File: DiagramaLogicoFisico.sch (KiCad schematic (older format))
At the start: 46 parts, among them J1 Conn_01x02_Servo1, J10 Conn_01x04_TRIS, J11 Conn_01x02_DSP, J2 Conn_01x03_UART1, J3 Conn_01x03_UART2, J4 Conn_01x04_PWM, J5 Conn_01x05_PROGRAMER, J6 Conn_01x02_POWER, J7 Conn_01x02_Servo2, J8 Conn_01x02_Servo3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

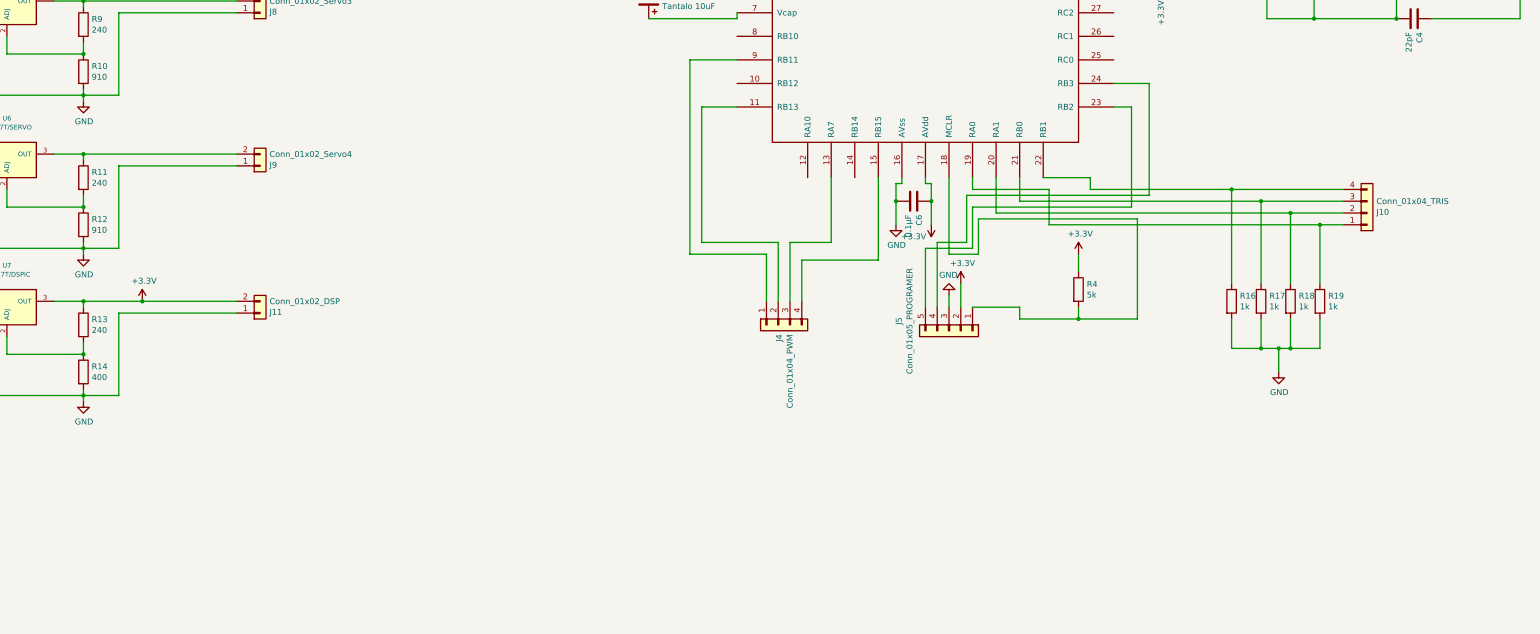
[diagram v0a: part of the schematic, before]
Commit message: Añadido los circuitos de interruptores y sus pines de alimentación
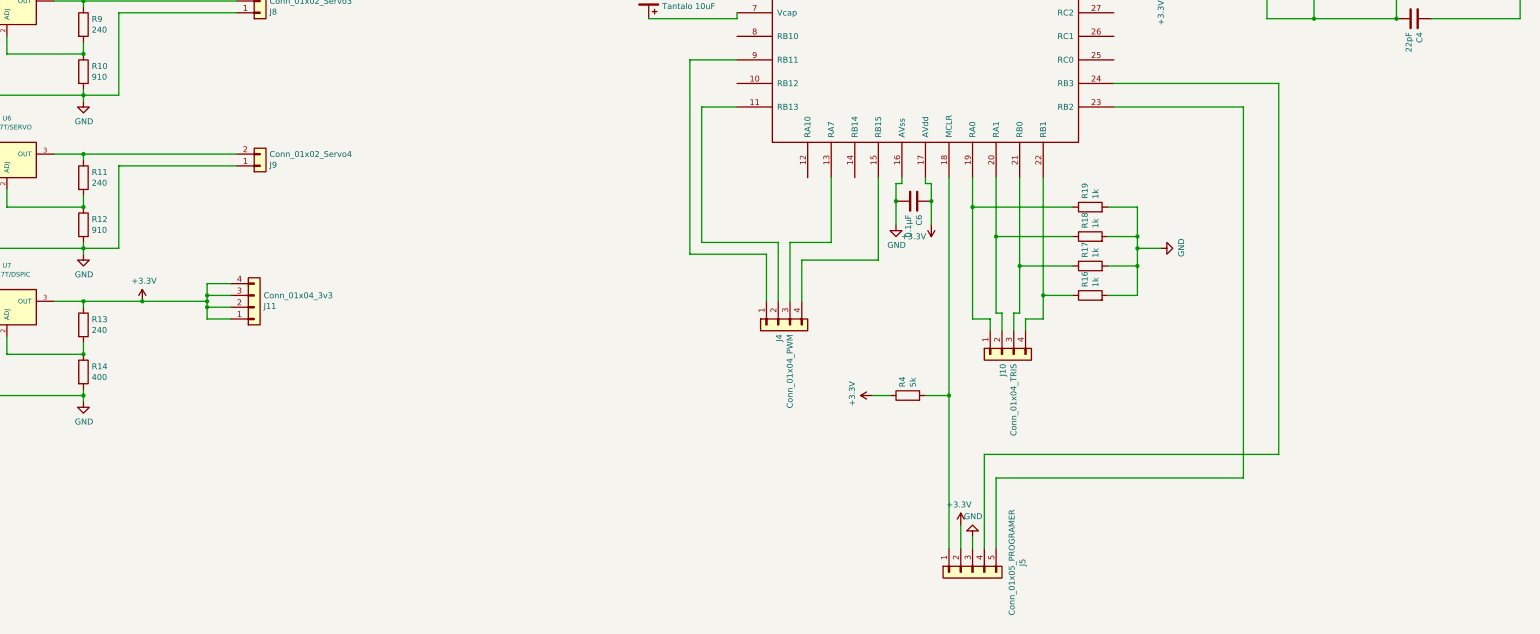
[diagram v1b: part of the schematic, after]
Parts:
- removed J11: Conn_01x02_DSP, TerminalBlock:TerminalBlock_bornier-2_P5.08mm, symbol Connector_Generic:Conn_01x02
- added J11: Conn_01x04_3v3, Connector_PinHeader_2.54mm:PinHeader_1x04_P2.54mm_Vertical, symbol Connector_Generic:Conn_01x04
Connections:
- net +3V3: now also J11.1 (Pin_1), J11.2 (Pin_2), J11.3 (Pin_3), J11.4 (Pin_4)
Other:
- moved on the sheet: J10, J5, R16, R17, R18, R19, R4

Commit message: añadidas algunas modifiaciones
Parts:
- added J?: Conn_01x04_TRIS, Connector_PinHeader_2.54mm:PinHeader_1x04_P2.54mm_Vertical, symbol Connector_Generic:Conn_01x04
- added JP? (x4): Jumper, symbol Device:Jumper
- added R? (x4): 1k, Resistor_THT:R_Axial_DIN0204_L3.6mm_D1.6mm_P5.08mm_Horizontal, symbol Device:R
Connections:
- net +3V3: now also JP?.1, JP?.1, JP?.1, JP?.1
- net GND: now also J?.1 (Pin_1), J?.2 (Pin_2), J?.3 (Pin_3), J?.4 (Pin_4), R?.1, R?.1, R?.1, R?.1
- new net: JP?.2, R?.2 (x4)
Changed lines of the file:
@@
 	10400 14150 10400 14250
 Connection ~ 10400 14250
+$Comp
+L Device:Jumper JP?
+U 1 1 5EFD7640
+P 21950 3550
+F 0 "JP?" H 21950 3814 50  0000 C CNN
+F 1 "Jumper" H 21950 3723 50  0000 C CNN
+F 2 "" H 21950 3550 50  0001 C CNN
+F 3 "~" H 21950 3550 50  0001 C CNN
+	1    21950 3550
+	0    1    1    0
+$EndComp
+$Comp
+L power:GND #PWR?
+U 1 1 5EFF4984
+P 22750 4900
+F 0 "#PWR?" H 22750 4650 50  0001 C CNN
+F 1 "GND" H 22755 4727 50  0000 C CNN
+F 2 "" H 22750 4900 50  0001 C CNN
+F 3 "" H 22750 4900 50  0001 C CNN
+	1    22750 4900
+	1    0    0    -1
+$EndComp
+$Comp
+L Device:R R?
+U 1 1 5F003B7F
+P 21950 4150
+F 0 "R?" H 22020 4196 50  0000 L CNN
+F 1 "1k" H 22020 4105 50  0000 L CNN
+F 2 "Resistor_THT:R_Axial_DIN0204_L3.6mm_D1.6mm_P5.08mm_Horizontal" V 21880 4150 50  0001 C CNN
+F 3 "~" H 21950 4150 50  0001 C CNN
+	1    21950 4150
+	-1   0    0    1
+$EndComp
+Wire Wire Line
+	21950 4000 21950 3850
+$Comp
+L power:+3.3V #PWR?
+U 1 1 5F085C7E
+P 22750 2900
+F 0 "#PWR?" H 22750 2750 50  0001 C CNN
+F 1 "+3.3V" H 22900 3000 50  0000 C CNN
+F 2 "" H 22750 2900 50  0001 C CNN
+F 3 "" H 22750 2900 50  0001 C CNN
+	1    22750 2900
+	1    0    0    -1
+$EndComp
+$Comp
+L Device:Jumper JP?
+U 1 1 5F0B49E5
+P 22500 3550
+F 0 "JP?" H 22500 3814 50  0000 C CNN
+F 1 "Jumper" H 22500 3723 50  0000 C CNN
+F 2 "" H 22500 3550 50  0001 C CNN
+F 3 "~" H 22500 3550 50  0001 C CNN
+	1    22500 3550
+	0    1    1    0
+$EndComp
+$Comp
+L Device:R R?
+U 1 1 5F0B49EB
+P 22500 4150
+F 0 "R?" H 22570 4196 50  0000 L CNN
+F 1 "1k" H 22570 4105 50  0000 L CNN
+F 2 "Resistor_THT:R_Axial_DIN0204_L3.6mm_D1.6mm_P5.08mm_Horizontal" V 22430 4150 50  0001 C CNN
+F 3 "~" H 22500 4150 50  0001 C CNN
+	1    22500 4150
+	-1   0    0    1
+$EndComp
+Wire Wire Line
+	22500 4000 22500 3850
+$Comp
+L Device:Jumper JP?
+U 1 1 5F0C321D
+P 22950 3550
+F 0 "JP?" H 22950 3814 50  0000 C CNN
+F 1 "Jumper" H 22950 3723 50  0000 C CNN
+F 2 "" H 22950 3550 50  0001 C CNN
+F 3 "~" H 22950 3550 50  0001 C CNN
+	1    22950 3550
+	0    1    1    0
+$EndComp
+$Comp
+L Device:R R?
+U 1 1 5F0C3223
+P 22950 4150
+F 0 "R?" H 23020 4196 50  0000 L CNN
+F 1 "1k" H 23020 4105 50  0000 L CNN
+F 2 "Resistor_THT:R_Axial_DIN0204_L3.6mm_D1.6mm_P5.08mm_Horizontal" V 22880 4150 50  0001 C CNN
+F 3 "~" H 22950 4150 50  0001 C CNN
+	1    22950 4150
+	-1   0    0    1
+$EndComp
+Wire Wire Line
+	22950 4000 22950 3850
+$Comp
+L Device:Jumper JP?
+U 1 1 5F0D216C
+P 23350 3550
+F 0 "JP?" H 23350 3814 50  0000 C CNN
+F 1 "Jumper" H 23350 3723 50  0000 C CNN
+F 2 "" H 23350 3550 50  0001 C CNN
+F 3 "~" H 23350 3550 50  0001 C CNN
+	1    23350 3550
+	0    1    1    0
+$EndComp
+$Comp
+L Device:R R?
+U 1 1 5F0D2172
+P 23350 4150
+F 0 "R?" H 23420 4196 50  0000 L CNN
+F 1 "1k" H 23420 4105 50  0000 L CNN
+F 2 "Resistor_THT:R_Axial_DIN0204_L3.6mm_D1.6mm_P5.08mm_Horizontal" V 23280 4150 50  0001 C CNN
+F 3 "~" H 23350 4150 50  0001 C CNN
+	1    23350 4150
+	-1   0    0    1
+$EndComp
+Wire Wire Line
+	23350 4000 23350 3850
+Wire Wire Line
+	22750 2900 22500 2900
+Wire Wire Line
+	21950 2900 21950 3250
+Wire Wire Line
+	22750 2900 22950 2900
+Wire Wire Line
+	23350 2900 23350 3250
+Connection ~ 22750 2900
+Wire Wire Line
+	22500 3250 22500 2900
+Connection ~ 22500 2900
+Wire Wire Line
+	22500 2900 21950 2900
+Wire Wire Line
+	22950 3250 22950 2900
+Connection ~ 22950 2900
+Wire Wire Line
+	22950 2900 23350 2900
+Wire Wire Line
+	21950 4900 22500 4900
+Wire Wire Line
+	21950 4300 21950 4400
+Wire Wire Line
+	22500 4300 22500 4500
+Connection ~ 22500 4900
+Wire Wire Line
+	22500 4900 22750 4900
+Wire Wire Line
+	22750 4900 22950 4900
+Wire Wire Line
+	23350 4300 23350 4700
+Connection ~ 22750 4900
+Wire Wire Line
+	22950 4300 22950 4600
+Connection ~ 22950 4900
+Wire Wire Line
+	22950 4900 23350 4900
+$Comp
+L Connector_Generic:Conn_01x04 J?
+U 1 1 5F1AC96A
+P 23950 4600
+F 0 "J?" H 24030 4592 50  0000 L CNN
+F 1 "Conn_01x04_TRIS" H 24030 4501 50  0000 L CNN
+F 2 "Connector_PinHeader_2.54mm:PinHeader_1x04_P2.54mm_Vertical" H 23950 4600 50  0001 C CNN
+F 3 "~" H 23950 4600 50  0001 C CNN
+	1    23950 4600
+	1    0    0    1
+$EndComp
+Wire Wire Line
+	23750 4400 21950 4400
+Connection ~ 21950 4400
+Wire Wire Line
+	21950 4400 21950 4900
+Wire Wire Line
+	23750 4500 22500 4500
+Connection ~ 22500 4500
+Wire Wire Line
+	22500 4500 22500 4900
+Wire Wire Line
+	23750 4600 22950 4600
+Connection ~ 22950 4600
+Wire Wire Line
+	22950 4600 22950 4900
+Wire Wire Line
+	23750 4700 23350 4700
+Connection ~ 23350 4700
+Wire Wire Line
+	23350 4700 23350 4900
 $EndSCHEMATC

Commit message: Sustituido el regulador del dspic
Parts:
- removed J?: Conn_01x04_TRIS, Connector_PinHeader_2.54mm:PinHeader_1x04_P2.54mm_Vertical, symbol Connector_Generic:Conn_01x04
- removed JP? (x4): Jumper, symbol Device:Jumper
- removed R13: 240, Resistor_THT:R_Axial_DIN0204_L3.6mm_D1.6mm_P5.08mm_Horizontal, symbol Device:R
- removed R14: 400, Resistor_THT:R_Axial_DIN0204_L3.6mm_D1.6mm_P5.08mm_Horizontal, symbol Device:R
- removed R? (x4): 1k, Resistor_THT:R_Axial_DIN0204_L3.6mm_D1.6mm_P5.08mm_Horizontal, symbol Device:R
- removed U7: LM317T/DSPIC, Package_TO_SOT_THT:TO-220-3_Vertical, symbol NCP:LM317T
- added C10: 22uF, Capacitor_THT:C_Disc_D3.8mm_W2.6mm_P2.50mm, symbol Device:C
- added C2: 0.33uF, Capacitor_THT:C_Disc_D3.8mm_W2.6mm_P2.50mm, symbol Device:C
- added C7: 0.1uF, Capacitor_THT:C_Disc_D3.8mm_W2.6mm_P2.50mm, symbol Device:C
- added C9: 10uF, Capacitor_THT:C_Disc_D3.8mm_W2.6mm_P2.50mm, symbol Device:C
- added U1: L7805, Package_TO_SOT_THT:TO-220-3_Vertical, symbol Regulator_Linear:L7805
- added U7: AZ1117-3.3, Package_TO_SOT_SMD:SOT-223-3_TabPin2, symbol Regulator_Linear:AZ1117-3.3
- U3, U4, U5, U6: symbol NCP:LM317T -> DiagramaLogicoFisico-rescue:LM317T-NCP
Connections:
- net +3V3: now also C10.1, U7.2 (VO)
- net GND: now also C10.2, C2.2, C7.2, C9.2, U1.2 (GND), U7.1 (GND)
- net at J6.2 (Pin_2), U3.1 (IN), U4.1 (IN)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: now also C2.1, U1.1 (IN)
- new net: C7.1, C9.1, U1.3 (OUT), U7.3 (VI)
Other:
- moved on the sheet: J11

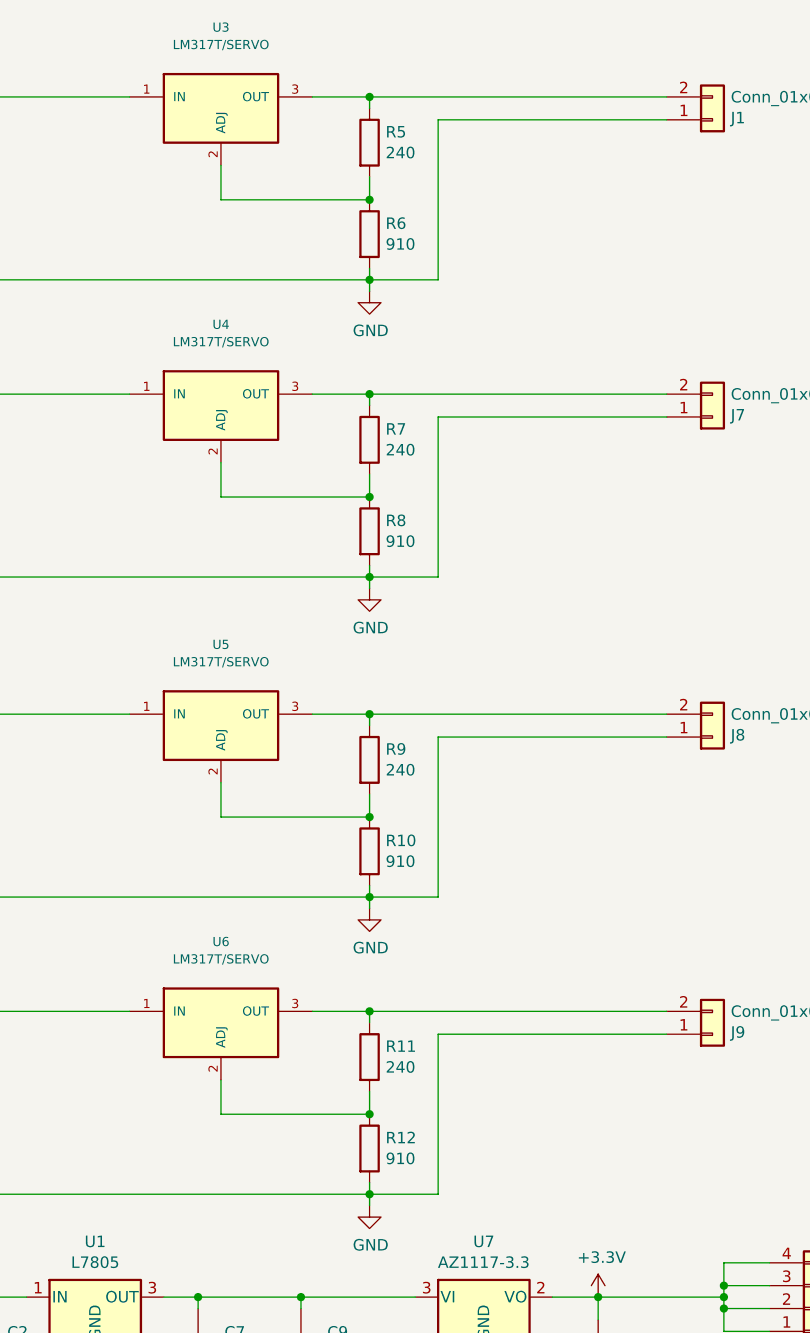
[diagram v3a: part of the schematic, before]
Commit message: Corregidos los valores de resistencias de los LM317 y alejado el regulador del dspic
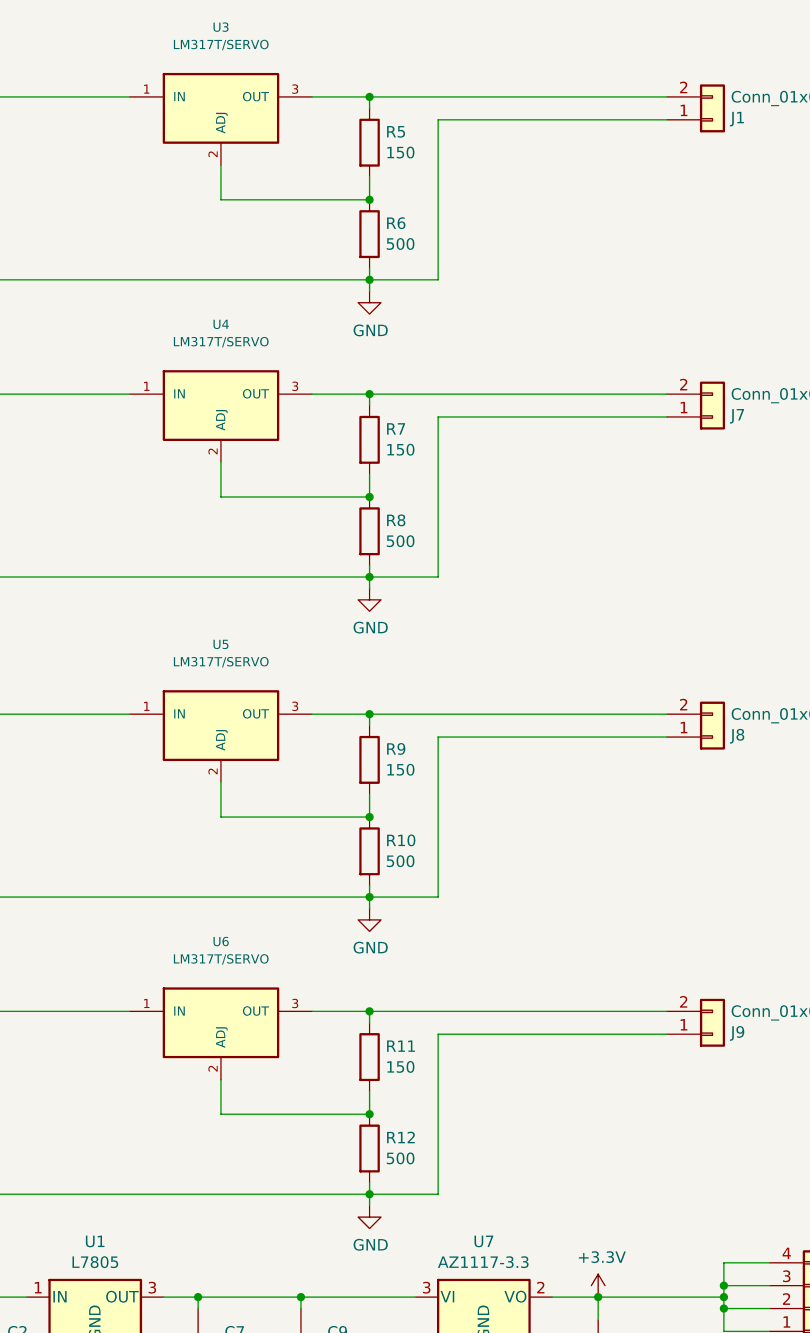
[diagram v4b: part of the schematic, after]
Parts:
- R10, R12, R6, R8: value 910 -> 500
- R11, R5, R7, R9: value 240 -> 150
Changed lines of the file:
@@
 P 9350 9650
 F 0 "R6" H 9420 9696 50  0000 L CNN
-F 1 "910" H 9420 9605 50  0000 L CNN
+F 1 "500" H 9420 9605 50  0000 L CNN
 F 2 "Resistor_THT:R_Axial_DIN0204_L3.6mm_D1.6mm_P5.08mm_Horizontal" V 9280 9650 50  0001 C CNN
 F 3 "~" H 9350 9650 50  0001 C CNN
@@
 P 9350 9250
 F 0 "R5" H 9420 9296 50  0000 L CNN
-F 1 "240" H 9420 9205 50  0000 L CNN
+F 1 "150" H 9420 9205 50  0000 L CNN
 F 2 "Resistor_THT:R_Axial_DIN0204_L3.6mm_D1.6mm_P5.08mm_Horizontal" V 9280 9250 50  0001 C CNN
 F 3 "~" H 9350 9250 50  0001 C CNN
@@
 P 9350 13650
 F 0 "R12" H 9420 13696 50  0000 L CNN
-F 1 "910" H 9420 13605 50  0000 L CNN
+F 1 "500" H 9420 13605 50  0000 L CNN
 F 2 "Resistor_THT:R_Axial_DIN0204_L3.6mm_D1.6mm_P5.08mm_Horizontal" V 9280 13650 50  0001 C CNN
 F 3 "~" H 9350 13650 50  0001 C CNN
@@
 P 9350 13250
 F 0 "R11" H 9420 13296 50  0000 L CNN
-F 1 "240" H 9420 13205 50  0000 L CNN
+F 1 "150" H 9420 13205 50  0000 L CNN
 F 2 "Resistor_THT:R_Axial_DIN0204_L3.6mm_D1.6mm_P5.08mm_Horizontal" V 9280 13250 50  0001 C CNN
 F 3 "~" H 9350 13250 50  0001 C CNN
@@
 P 9350 12350
 F 0 "R10" H 9420 12396 50  0000 L CNN
-F 1 "910" H 9420 12305 50  0000 L CNN
+F 1 "500" H 9420 12305 50  0000 L CNN
 F 2 "Resistor_THT:R_Axial_DIN0204_L3.6mm_D1.6mm_P5.08mm_Horizontal" V 9280 12350 50  0001 C CNN
 F 3 "~" H 9350 12350 50  0001 C CNN
@@
 P 9350 11950
 F 0 "R9" H 9420 11996 50  0000 L CNN
-F 1 "240" H 9420 11905 50  0000 L CNN
+F 1 "150" H 9420 11905 50  0000 L CNN
 F 2 "Resistor_THT:R_Axial_DIN0204_L3.6mm_D1.6mm_P5.08mm_Horizontal" V 9280 11950 50  0001 C CNN
 F 3 "~" H 9350 11950 50  0001 C CNN
@@
 P 9350 10950
 F 0 "R8" H 9420 10996 50  0000 L CNN
-F 1 "910" H 9420 10905 50  0000 L CNN
+F 1 "500" H 9420 10905 50  0000 L CNN
 F 2 "Resistor_THT:R_Axial_DIN0204_L3.6mm_D1.6mm_P5.08mm_Horizontal" V 9280 10950 50  0001 C CNN
 F 3 "~" H 9350 10950 50  0001 C CNN
@@
 P 9350 10550
 F 0 "R7" H 9420 10596 50  0000 L CNN
-F 1 "240" H 9420 10505 50  0000 L CNN
+F 1 "150" H 9420 10505 50  0000 L CNN
 F 2 "Resistor_THT:R_Axial_DIN0204_L3.6mm_D1.6mm_P5.08mm_Horizontal" V 9280 10550 50  0001 C CNN
 F 3 "~" H 9350 10550 50  0001 C CNN
